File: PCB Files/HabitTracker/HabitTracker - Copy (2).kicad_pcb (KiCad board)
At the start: 2 copper layers, 39 parts, among them U1 TLC5955DCA, U2 DCA0056F_N, U3 DCA0056F_N

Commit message: Updated PCB
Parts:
- U2, U3: value DCA0056F_N -> TLC5955DCA
- moved U3 1.01 mm to (199.9, 130.3)
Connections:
- U2 pad 1: /SERIAL_IN -> /SERIAL_LINK1
- U2 pad 28: /SERIAL_LINK1 -> /SERIAL_LINK2
- U3 pad 1: /SERIAL_IN -> /SERIAL_LINK2
- U3 pad 28: /SERIAL_LINK1 -> /SERIAL_OUT
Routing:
- net +5V: track 741.5 -> 4.73 mm, vias 3 -> 1
- net /GS_CLOCK: track 173.1 -> 3.55 mm, vias 0 -> 1
- net /SERIAL_IN: track 154.5 -> 0.00 mm, vias 2 -> 0
- net GND: track 140.8 -> 47.3 mm, vias 0 -> 36
- net /SERIAL_LINK1: track 117.8 -> 50.2 mm, vias 3 -> 2
- net /SERIAL_LINK2: track 0.00 -> 47.6 mm, vias 0 -> 2
- net /SERIAL_CLOCK: track 157.3 -> 125.0 mm, vias 0 -> 3
- net /LATCH: track 159.4 -> 128.1 mm, vias 0 -> 3
- net Net-(LED25-Pad5): track 15.1 -> 33.6 mm
- net Net-(LED25-Pad4): track 17.7 -> 35.3 mm
- net Net-(LED35-Pad6): track 9.79 -> 26.2 mm
- net Net-(LED35-Pad5): track 13.1 -> 27.6 mm
- net Net-(LED25-Pad6): track 13.8 -> 28.1 mm
- net Net-(LED35-Pad4): track 14.9 -> 29.0 mm
- net Net-(LED19-Pad4): track 12.7 -> 25.2 mm
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- added copper zone on B.Cu, net GND

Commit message: First draft of PCB
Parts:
- added C1: 10uF, Capacitor_SMD:C_0805_2012Metric, F.Cu at (102.7, 132.3)
- added C2: 10uF, Capacitor_SMD:C_0805_2012Metric, F.Cu at (192.3, 132.6)
- added C3: 10uF, Capacitor_SMD:C_0805_2012Metric, F.Cu at (147.1, 106.7)
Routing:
- net /GS_CLOCK: track 3.55 -> 116.4 mm, vias 1 -> 3
- net /SERIAL_CLOCK: track 125.0 -> 141.1 mm
- net /LATCH: track 128.1 -> 139.9 mm
- net GND: track 47.3 -> 57.4 mm, vias 36 -> 39
- net /SERIAL_LINK2: track 47.6 -> 57.4 mm
- net /SERIAL_LINK1: track 50.2 -> 58.5 mm
- net Net-(LED25-Pad4): track 35.3 -> 30.3 mm
- net Net-(LED25-Pad5): track 33.6 -> 28.8 mm
- net Net-(LED19-Pad6): track 28.1 -> 24.0 mm
- net +5V: track 4.73 -> 8.78 mm, vias 1 -> 3
- net Net-(LED19-Pad4): track 25.2 -> 21.5 mm
- net Net-(LED19-Pad5): track 26.5 -> 23.0 mm
- net Net-(LED25-Pad6): track 28.1 -> 27.3 mm
- added copper zone on F.Cu, net +5V

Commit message: Added connector to PCB
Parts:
- added J1: Conn_01x10_Male, Connector_PinSocket_2.54mm:PinSocket_2x05_P2.54mm_Vertical, F.Cu at (149.6, 149.9)
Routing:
- net /LATCH: track 139.9 -> 236.4 mm
- net /SERIAL_IN: track 0.00 -> 92.2 mm, vias 0 -> 1
- net /SERIAL_CLOCK: track 141.1 -> 232.5 mm
- net /GS_CLOCK: track 116.4 -> 197.4 mm
- net /SERIAL_OUT: track 0.00 -> 68.5 mm, vias 0 -> 1

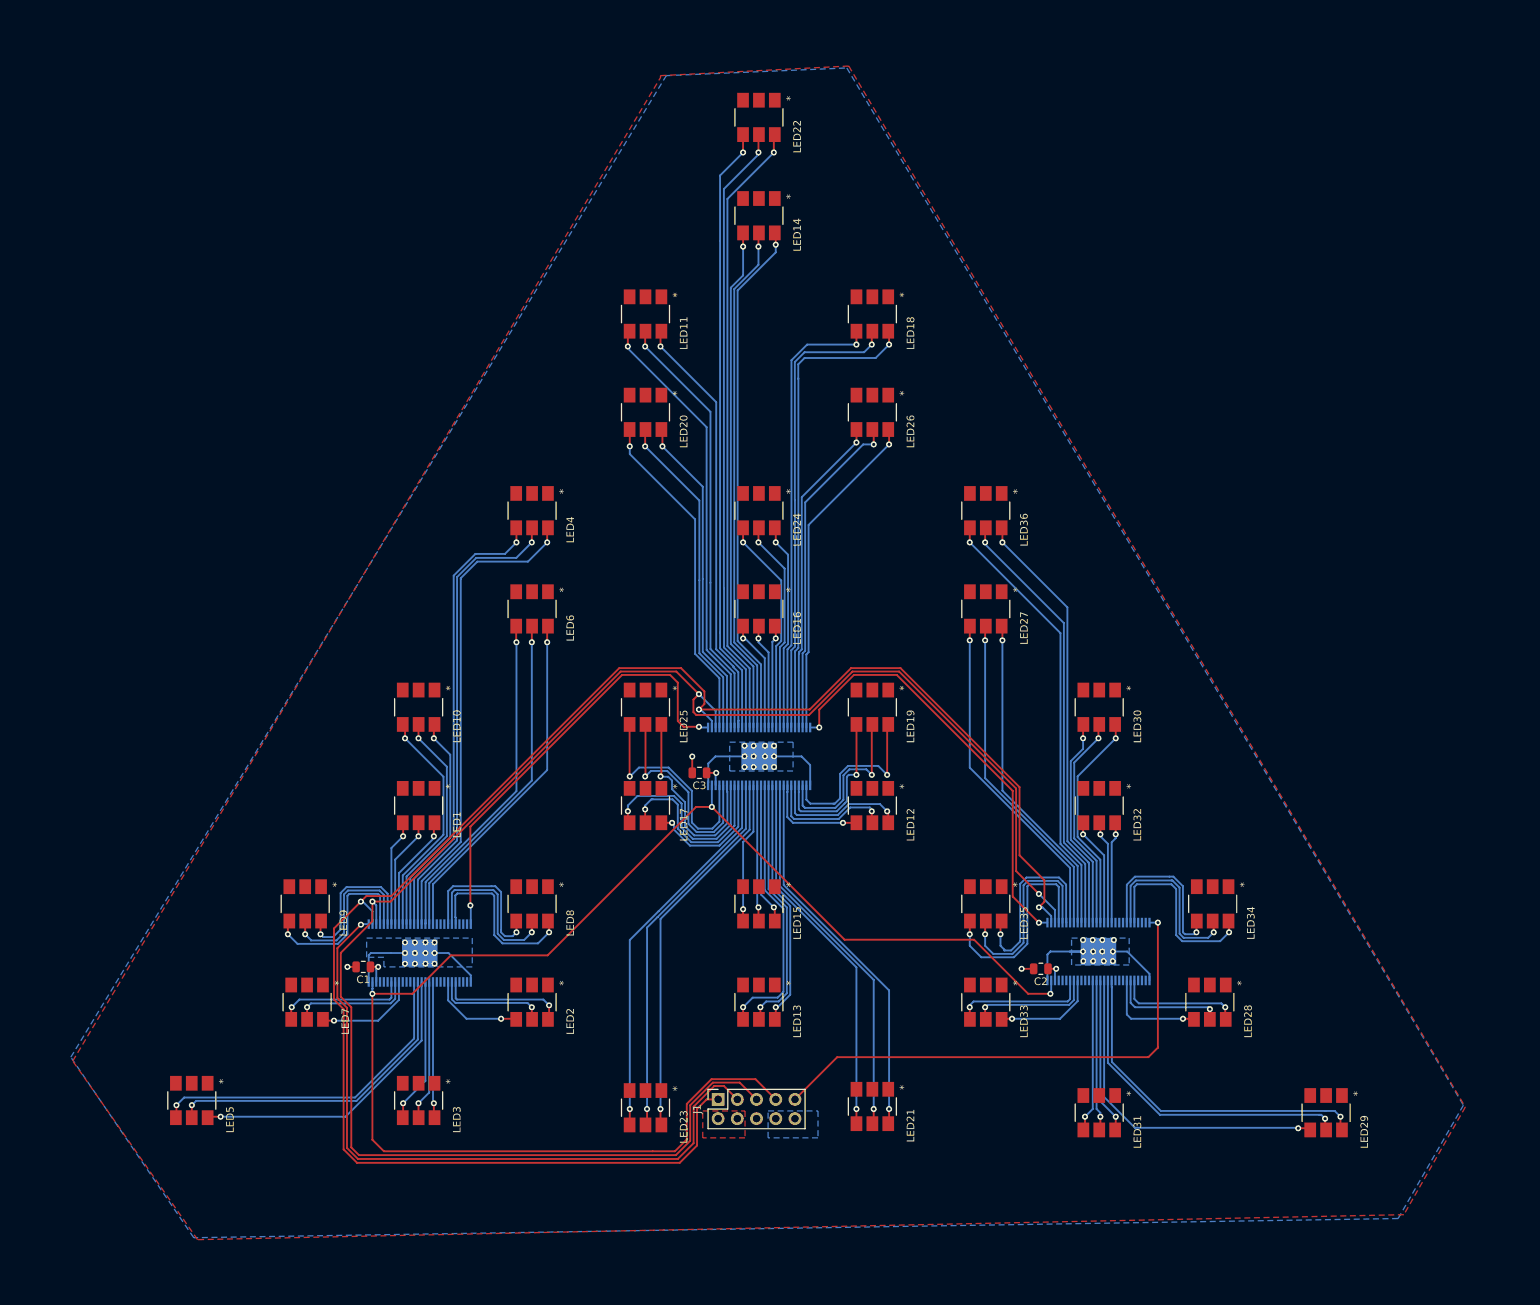
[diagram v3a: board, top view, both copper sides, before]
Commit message: Added border to PCB
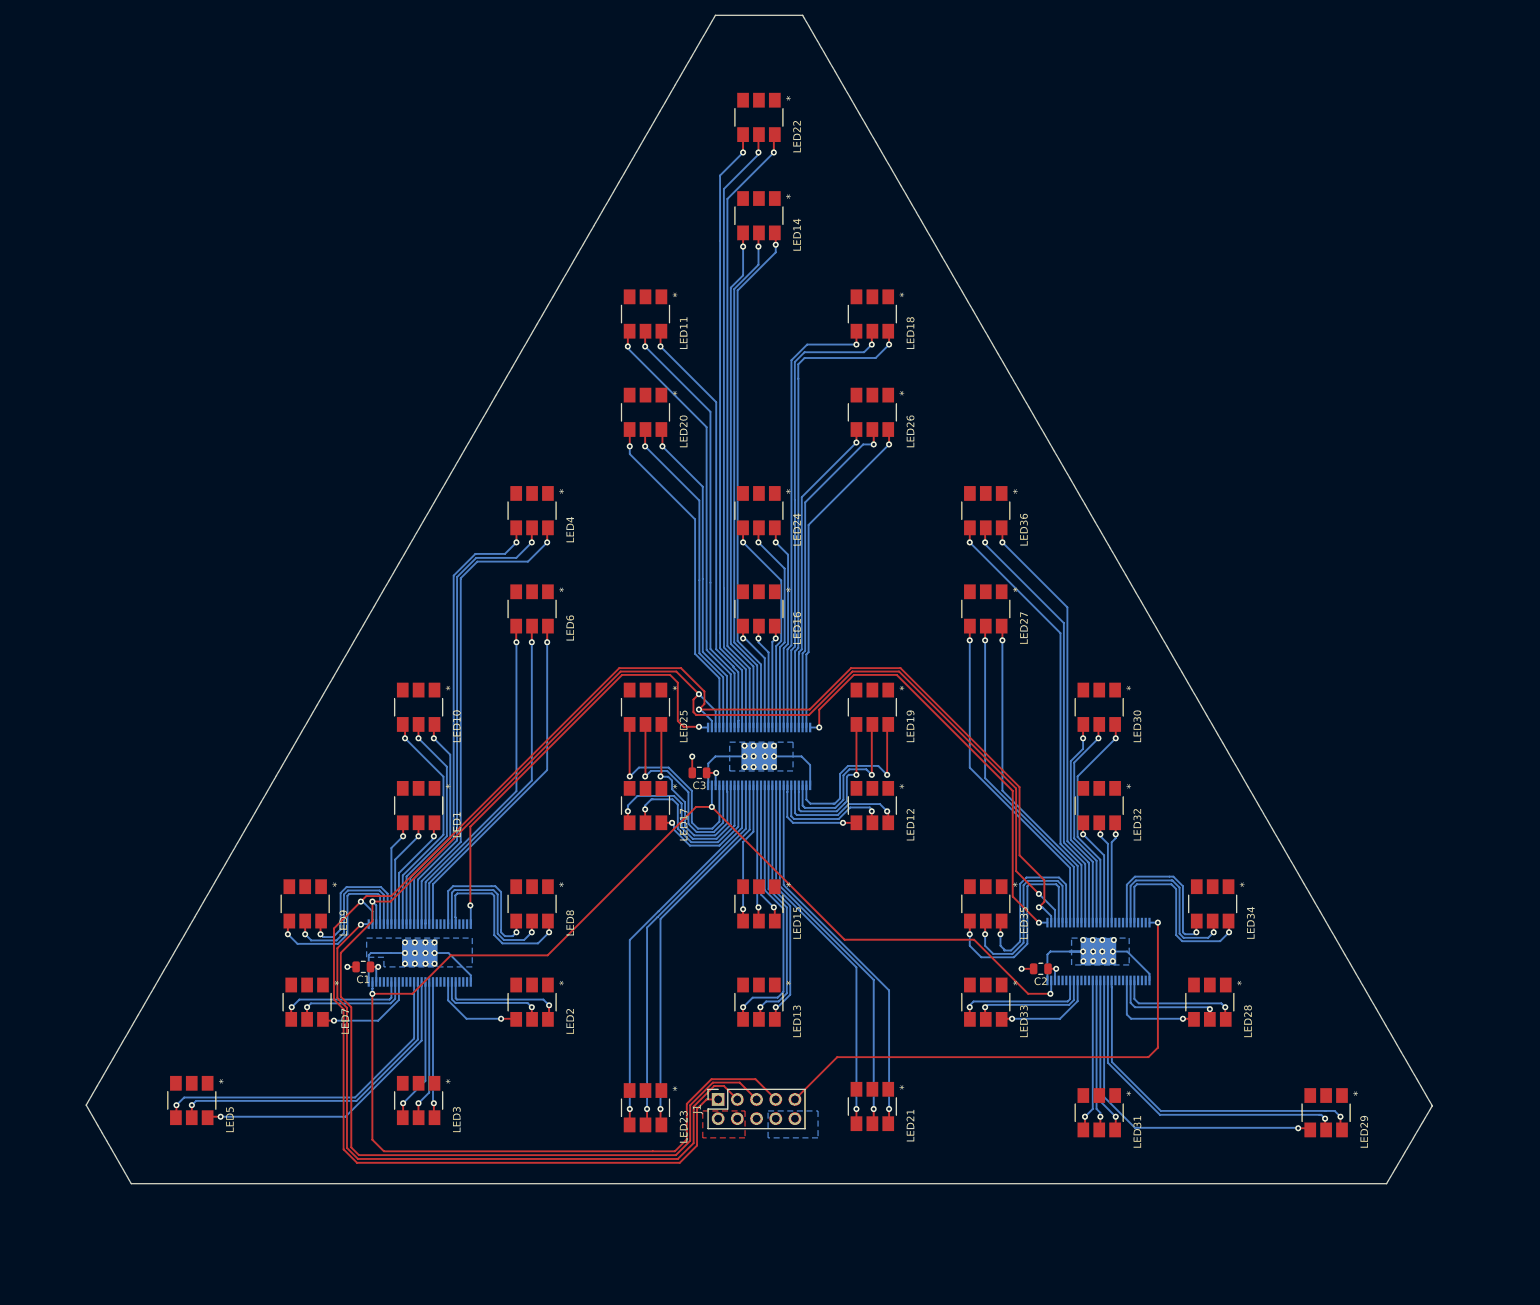
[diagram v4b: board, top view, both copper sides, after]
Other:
- board outline added: 178 x 154.5 mm

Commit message: Added power and ground planes
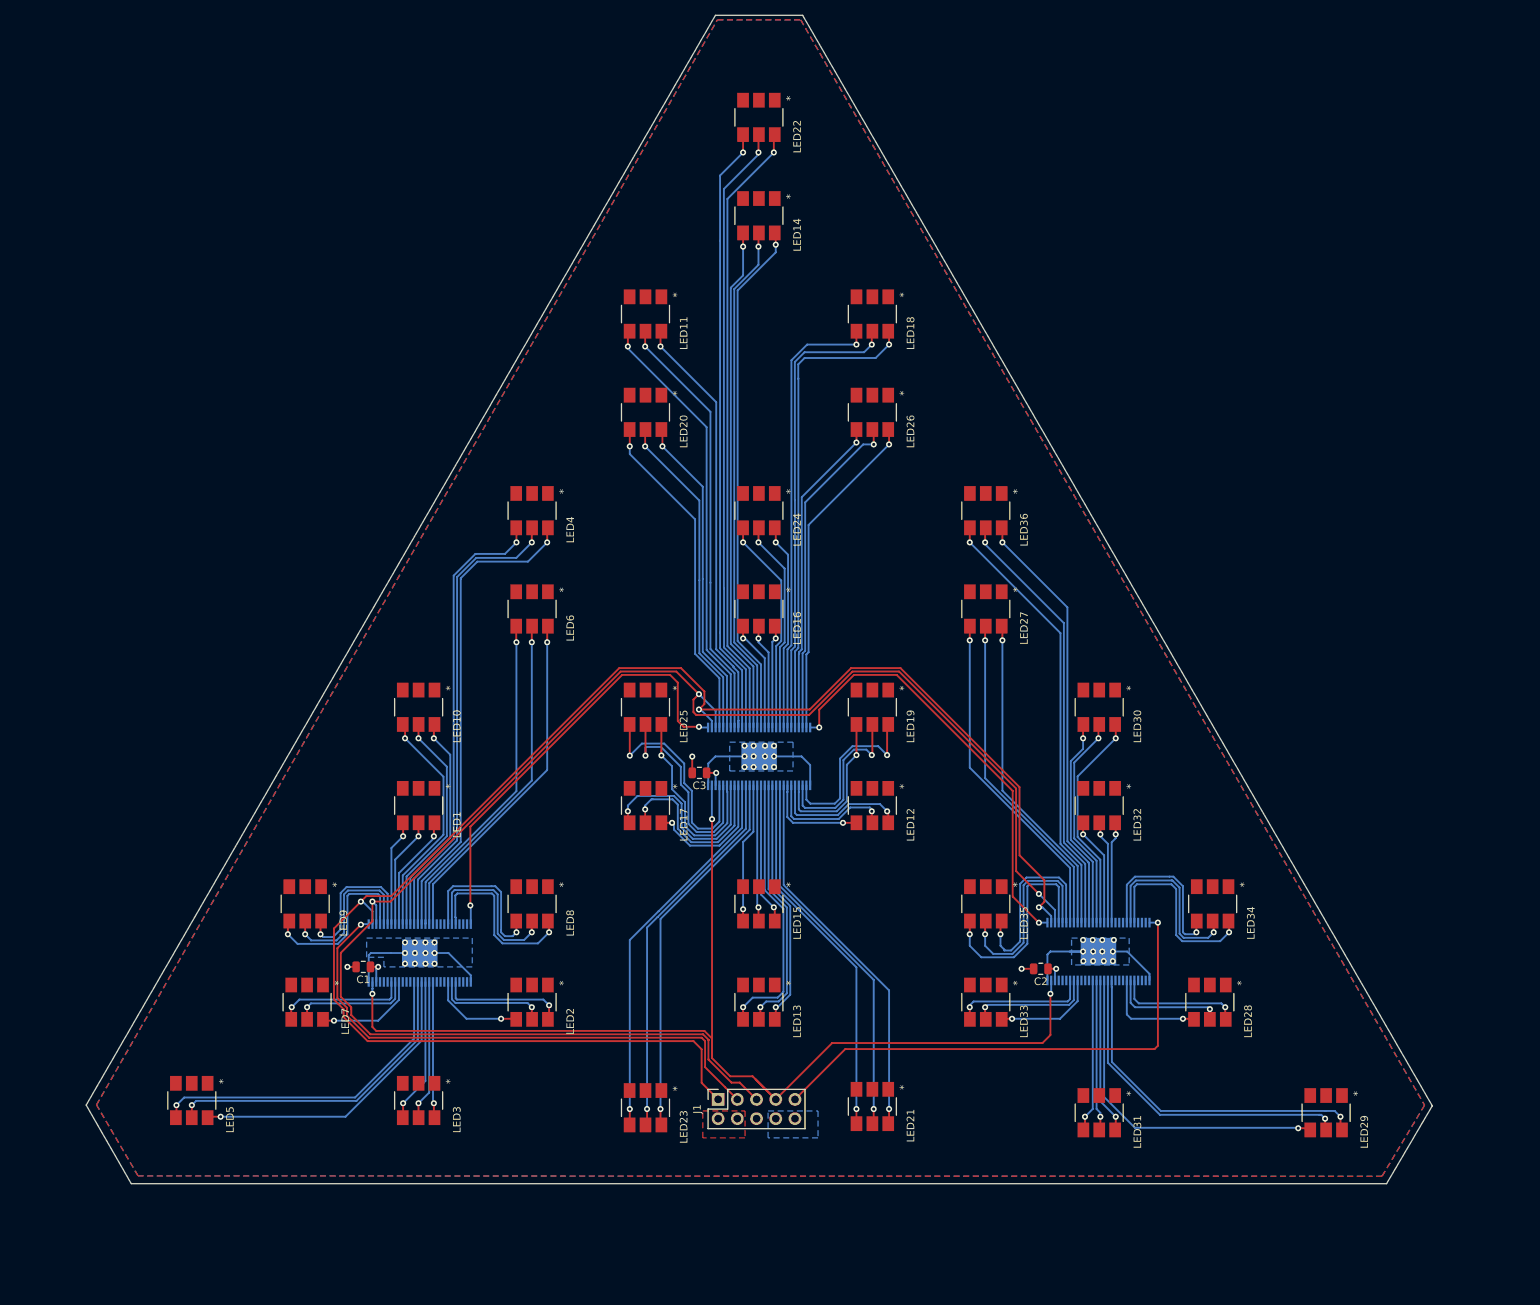
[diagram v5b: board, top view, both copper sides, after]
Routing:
- net /GS_CLOCK: track 197.4 -> 151.6 mm
- net /LATCH: track 236.4 -> 217.0 mm
- net /SERIAL_IN: track 92.2 -> 73.1 mm
- net /SERIAL_CLOCK: track 232.5 -> 215.0 mm
- net Net-(LED25-Pad6): track 27.3 -> 26.6 mm
- net Net-(LED25-Pad5): track 28.8 -> 29.4 mm
- net Net-(LED19-Pad4): track 21.5 -> 20.9 mm
